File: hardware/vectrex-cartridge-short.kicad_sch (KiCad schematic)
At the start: 16 parts, among them U2 DS2431+ TO-92

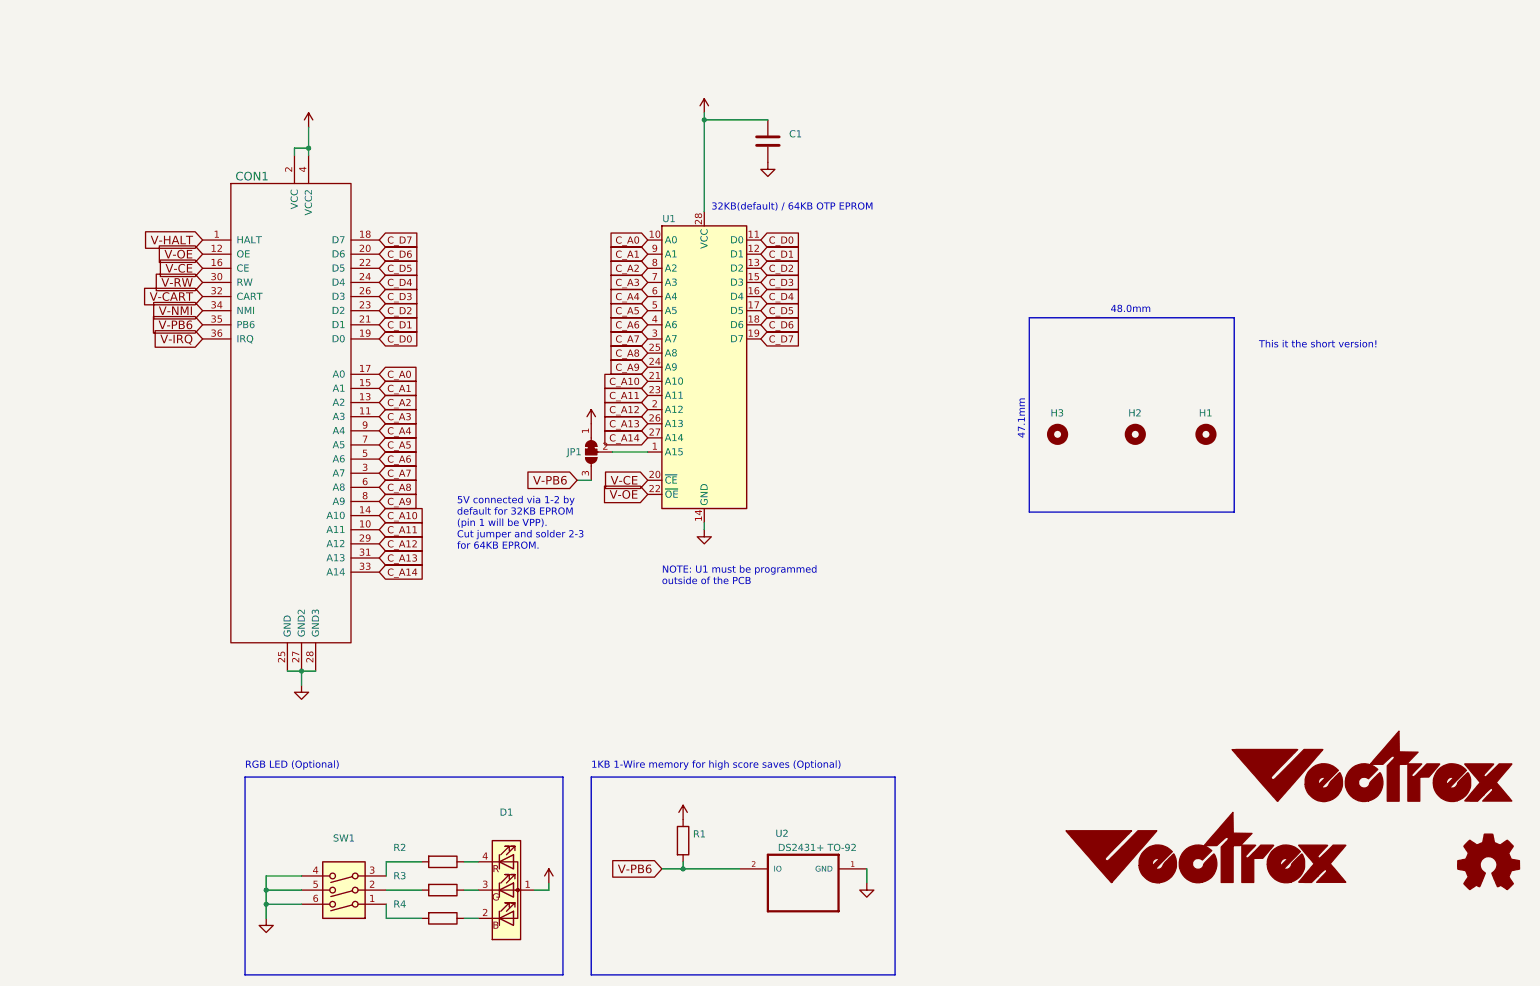
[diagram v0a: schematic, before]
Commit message: update RGB LED resistor values for deeper color
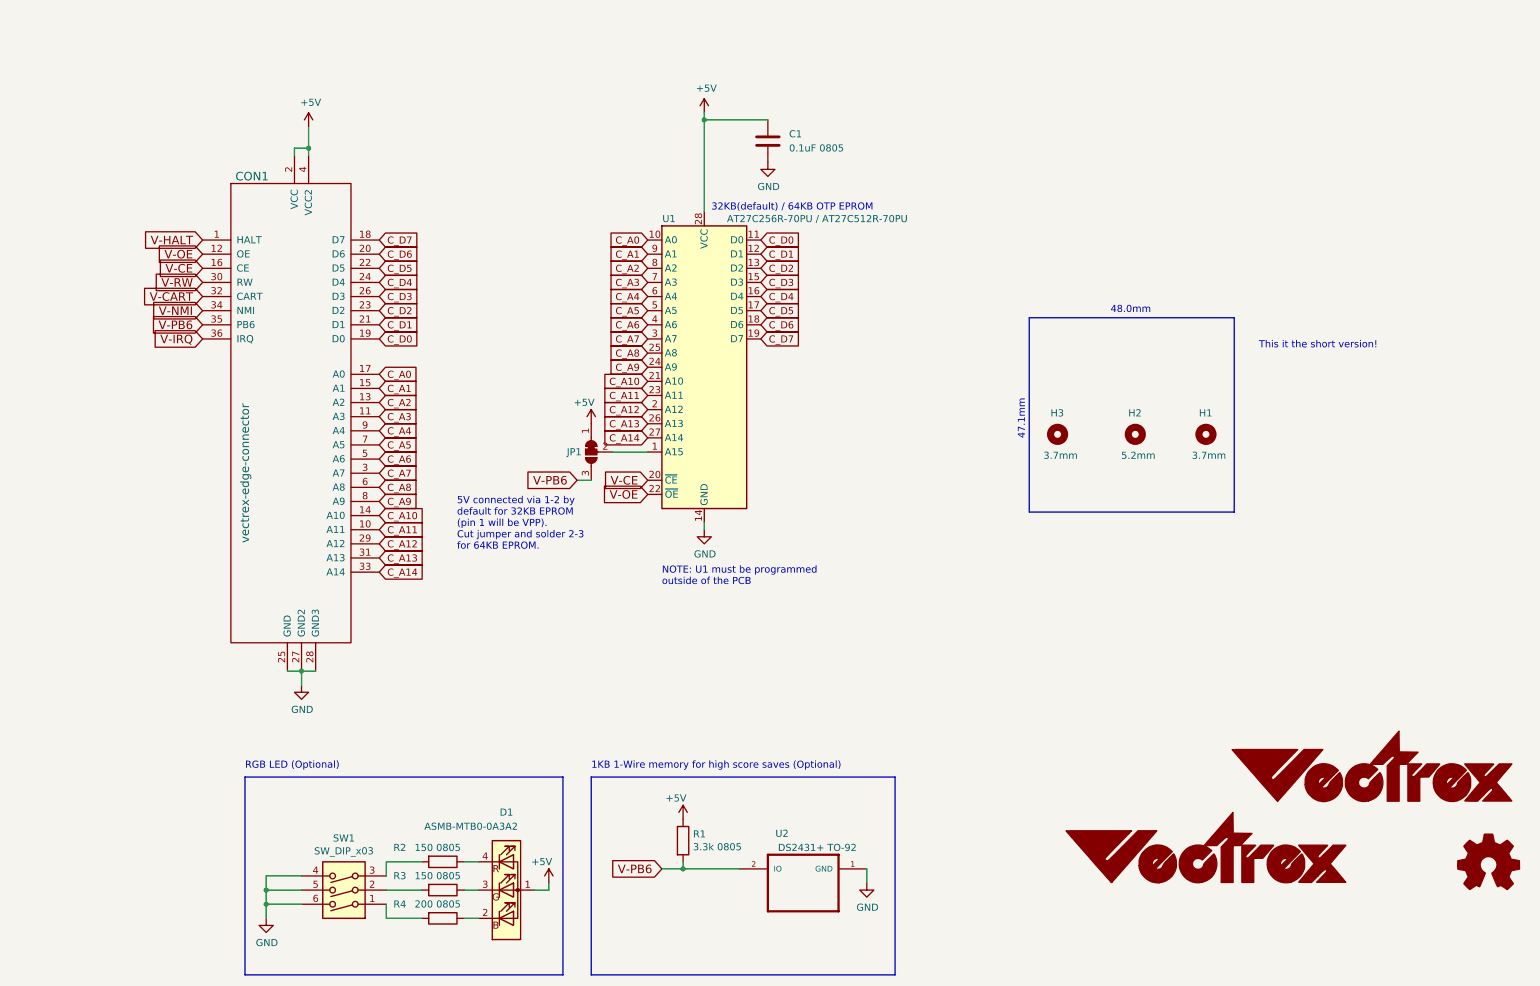
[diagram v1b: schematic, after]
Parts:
- C1: value (none) -> 0.1uF 0805; footprint (none) -> Capacitor_SMD:C_0805_2012Metric_Pad1.15x1.40mm_HandSolder
- CON1: value (none) -> vectrex-edge-connector; footprint (none) -> vectrex-cartridge:vectrex-edge-connector-thinner-no-soldermask
- D1: value (none) -> ASMB-MTB0-0A3A2; footprint (none) -> vectrex-cartridge:LED_Avago_PLCC4_3.2x2.8mm_CW
- G1: value (none) -> LOGO; footprint (none) -> vectrex-cartridge:vectrex-us-soldermask-37mm
- G2: value (none) -> LOGO; footprint (none) -> vectrex-cartridge:vectrex-us-soldermask-15mm
- H1, H3: value (none) -> 3.7mm; footprint (none) -> vectrex-cartridge:Mounting_Hole_D3.7mm
- H2: value (none) -> 5.2mm; footprint (none) -> vectrex-cartridge:Mounting_Hole_D5.2mm
- JP1: value (none) -> SolderJumper_3_Bridged12; footprint (none) -> vectrex-cartridge:SolderJumper-3_P1.3mm_Bridged12_RoundedPad1.0x1.5mm_NumberLabels
- R1: value (none) -> 3.3k 0805; footprint (none) -> Resistor_SMD:R_0805_2012Metric_Pad1.15x1.40mm_HandSolder
- R2, R3: value (none) -> 150 0805; footprint (none) -> Resistor_SMD:R_0805_2012Metric_Pad1.15x1.40mm_HandSolder
- R4: value (none) -> 200 0805; footprint (none) -> Resistor_SMD:R_0805_2012Metric_Pad1.15x1.40mm_HandSolder
- SW1: value (none) -> SW_DIP_x03; footprint (none) -> Button_Switch_SMD:SW_DIP_SPSTx03_Slide_6.7x9.18mm_W8.61mm_P2.54mm_LowProfile
- U1: value (none) -> AT27C256R-70PU / AT27C512R-70PU; footprint (none) -> Package_DIP:DIP-28_W15.24mm

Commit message: update vectrex-cartridge-short to v1.4 all SMT
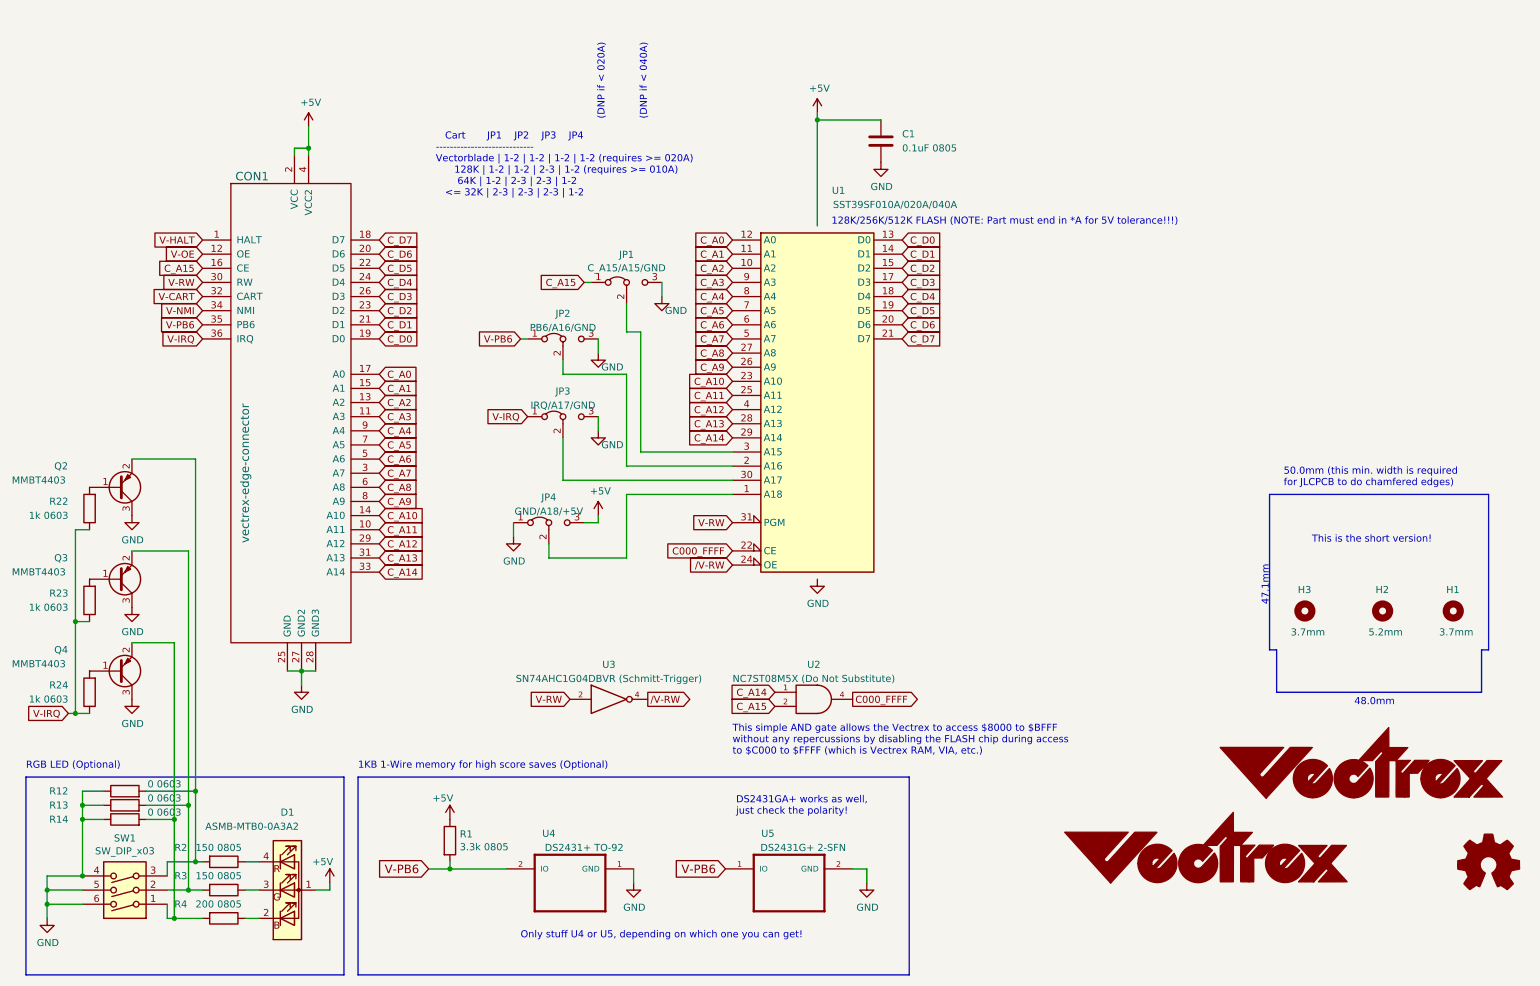
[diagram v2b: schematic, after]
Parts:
- removed JP1: SolderJumper_3_Bridged12, vectrex-cartridge:SolderJumper-3_P1.3mm_Bridged12_RoundedPad1.0x1.5mm_NumberLabels, symbol Jumper:SolderJumper_3_Bridged12
- removed U1: AT27C256R-70PU / AT27C512R-70PU, Package_DIP:DIP-28_W15.24mm, symbol Memory_EPROM:27C512
- added JP1: C_A15/A15/GND, vectrex-cartridge:R_0603_1608Metric_Jumper_12_Bridged, symbol Jumper:Jumper_3_Bridged12
- added JP2: PB6/A16/GND, vectrex-cartridge:R_0603_1608Metric_Jumper_12_Bridged, symbol Jumper:Jumper_3_Bridged12
- added JP3: IRQ/A17/GND, vectrex-cartridge:R_0603_1608Metric_Jumper_12_Bridged, symbol Jumper:Jumper_3_Bridged12
- added JP4: GND/A18/+5V, vectrex-cartridge:R_0603_1608Metric_Jumper_12_Bridged, symbol Jumper:Jumper_3_Bridged12
- added Q2, Q3, Q4: MMBT4403, Package_TO_SOT_SMD:SOT-23, symbol Transistor_BJT:MMBT3906
- added R12, R13, R14: 0 0603, Resistor_SMD:R_0603_1608Metric_Pad0.98x0.95mm_HandSolder, symbol Device:R
- added R22, R23, R24: 1k 0603, Resistor_SMD:R_0603_1608Metric_Pad0.98x0.95mm_HandSolder, symbol Device:R
- added U1: SST39SF010A/020A/040A, Package_LCC:PLCC-32_11.4x14.0mm_P1.27mm, symbol Memory_Flash:SST39SF040
- added U2: NC7ST08M5X (Do Not Substitute), Package_TO_SOT_SMD:SOT-23-5_HandSoldering, symbol 74xGxx:74AHC1G08
- added U3: SN74AHC1G04DBVR (Schmitt-Trigger), Package_TO_SOT_SMD:SOT-23-5_HandSoldering, symbol 74xGxx:74AHC1G04
- added U5: DS2431G+ 2-SFN, vectrex-cartridge:2SFN_6mmx6mm, symbol ds2431:DS2431
- CON1: footprint vectrex-cartridge:vectrex-edge-connector-thinner-no-soldermask -> vectrex-cartridge:vectrex-edge-connector-thinner-no-soldermask-no-silk
- G1: footprint vectrex-cartridge:vectrex-us-soldermask-37mm -> vectrex-cartridge:vectrex-us-soldermask-15mm
- G2: footprint vectrex-cartridge:vectrex-us-soldermask-15mm -> vectrex-cartridge:vectrex-us-silkscreen-15mm
- SW1: footprint Button_Switch_SMD:SW_DIP_SPSTx03_Slide_6.7x9.18mm_W8.61mm_P2.54mm_LowProfile -> vectrex-cartridge:SW_DIP_SPSTx03_Slide_6.7x9.18mm_W8.61mm_P2.54mm_LowProfile_NoSWSilk
- U4: renamed from U2; footprint vectrex-cartridge:TO-92_Inline_BW -> vectrex-cartridge:TO-92_Inline_BW_SMT
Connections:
- net +5V: now also JP4.3 (B), U1.32 (VCC), U2.5 (VCC), U3.5 (VCC)
- net C_A0: now also U1.12 (A0)
- net C_A1: now also U1.11 (A1)
- net C_A10: now also U1.23 (A10)
- net C_A11: now also U1.25 (A11)
- net C_A12: now also U1.4 (A12)
- net C_A13: now also U1.28 (A13)
- net C_A14: now also U1.29 (A14), U2.1
- net C_A2: now also U1.10 (A2)
- net C_A3: now also U1.9 (A3)
- net C_A4: now also U1.8 (A4)
- net C_A5: now also U1.7 (A5)
- net C_A6: now also U1.6 (A6)
- net C_A7: now also U1.5 (A7)
- net C_A8: now also U1.27 (A8)
- net C_A9: now also U1.26 (A9)
- net C_D0: now also U1.13 (D0)
- net C_D1: now also U1.14 (D1)
- net C_D2: now also U1.15 (D2)
- net C_D3: now also U1.17 (D3)
- net C_D4: now also U1.18 (D4)
- net C_D5: now also U1.19 (D5)
- net C_D6: now also U1.20 (D6)
- net C_D7: now also U1.21 (D7)
- net GND: now also JP1.3 (B), JP2.3 (B), JP3.3 (B), JP4.1 (A), Q2.3 (C), Q3.3 (C), Q4.3 (C), R12.1, R13.1, R14.1, U1.16 (GND), U2.3 (GND), U3.3 (GND), U5.2 (GND)
- net V-IRQ: now also JP3.1 (A), R22.1, R23.1, R24.1
- net V-PB6: now also JP2.1 (A), U5.1 (IO)
- net V-RW: now also U1.31 (PGM), U3.2
- net at R2.2, SW1.3: now also Q2.2 (E), R12.2
- net at R3.2, SW1.2: now also Q3.2 (E), R13.2
- net at R4.2, SW1.1: now also Q4.2 (E), R14.2
- net V-CE renamed C_A15
- net C_A15: now also JP1.1 (A), U2.2
- new net: JP4.2 (C), U1.1 (A18)
- new net: JP2.2 (C), U1.2 (A16)
- new net: JP1.2 (C), U1.3 (A15)
- new net: JP3.2 (C), U1.30 (A17)
- new net: Q3.1 (B), R23.2
- new net: Q2.1 (B), R22.2
- new net: Q4.1 (B), R24.2
- new net C000_FFFF: U1.22 (CE), U2.4
- new net /V-RW: U1.24 (OE), U3.4
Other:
- note added: "(DNP if < 020A)"
- note added: "(DNP if < 040A)"
- note added: "128K/256K/512K FLASH (NOTE: Part must end in *A for 5V tolerance!!!)"
- note added: "50.0mm (this min. width is required for JLCPCB to do chamfered edges)"
- note added: "Cart JP1 JP2 JP3 JP4 ---------------------------- Vectorblade | 1-2 | 1-2 | 1-2 | 1-2 (requires >= 020A) 128K | 1-2 | 1-2 | 2-3 | 1-2 (requires >= 010A) 64K | 1-2 | 2-3 | 2-3 | 1-2 <= 32K | 2-3 | 2-3 | 2-3 | 1-2"
- note added: "DS2431GA+ works as well, just check the polarity!"
- note added: "Only stuff U4 or U5, depending on which one you can get!"
- note added: "This is the short version!"
- note added: "This simple AND gate allows the Vectrex to access $8000 to $BFFF without any repercussions by disabling the FLASH chip during access to $C000 to $FFFF (which is Vectrex RAM, VIA, etc.)"
- note removed: "32KB(default) / 64KB OTP EPROM"
- note removed: "5V connected via 1-2 by default for 32KB EPROM (pin 1 will be VPP). Cut jumper and solder 2-3 for 64KB EPROM."
- note removed: "NOTE: U1 must be programmed outside of the PCB"
- note removed: "This it the short version!"
- moved on the sheet: D1, H1, H2, H3, R1, R2, R3, R4, SW1, U4
